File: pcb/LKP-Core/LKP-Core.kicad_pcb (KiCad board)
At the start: 2 copper layers, 41 x 32 mm, 30 parts, among them J1 Intercon L, J2 Intercon R, J3 Power JST PH, J4 IO, J5 SWD, U1 CY8C4246AZI-M445

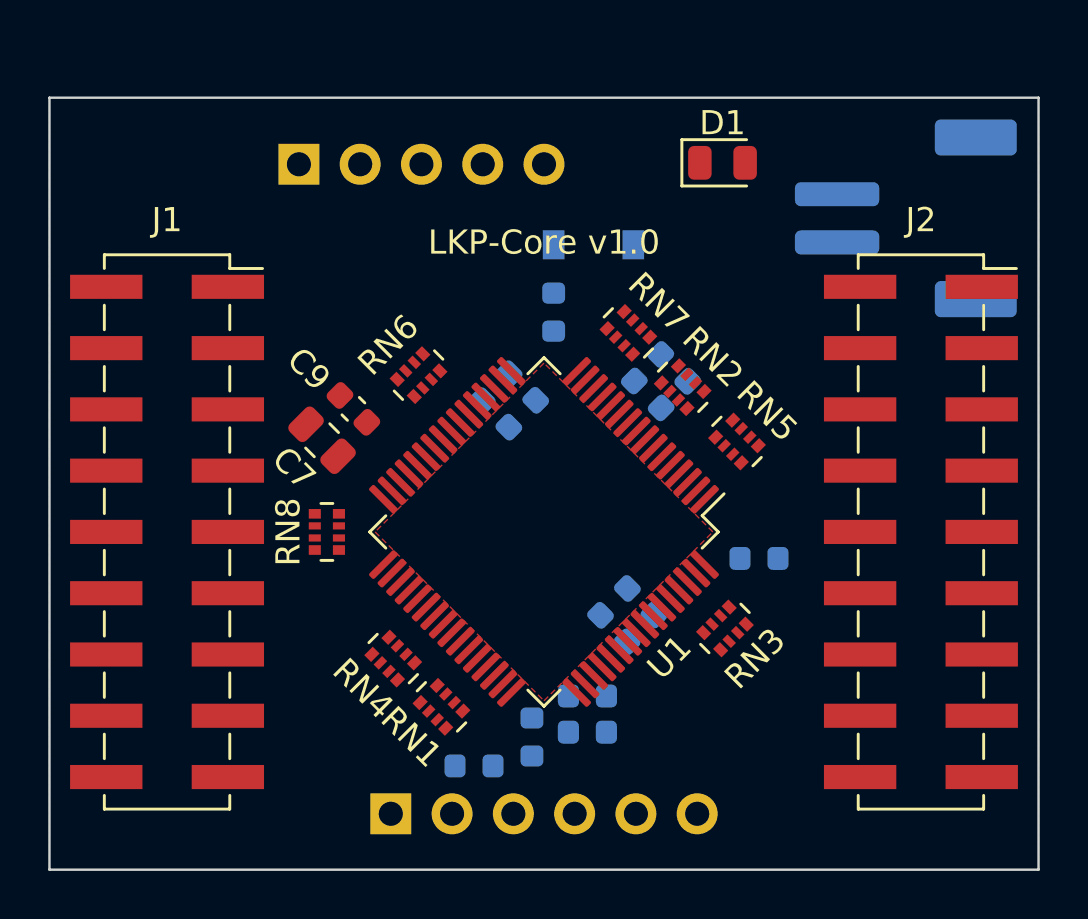
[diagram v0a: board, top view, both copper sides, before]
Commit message: Define net classes
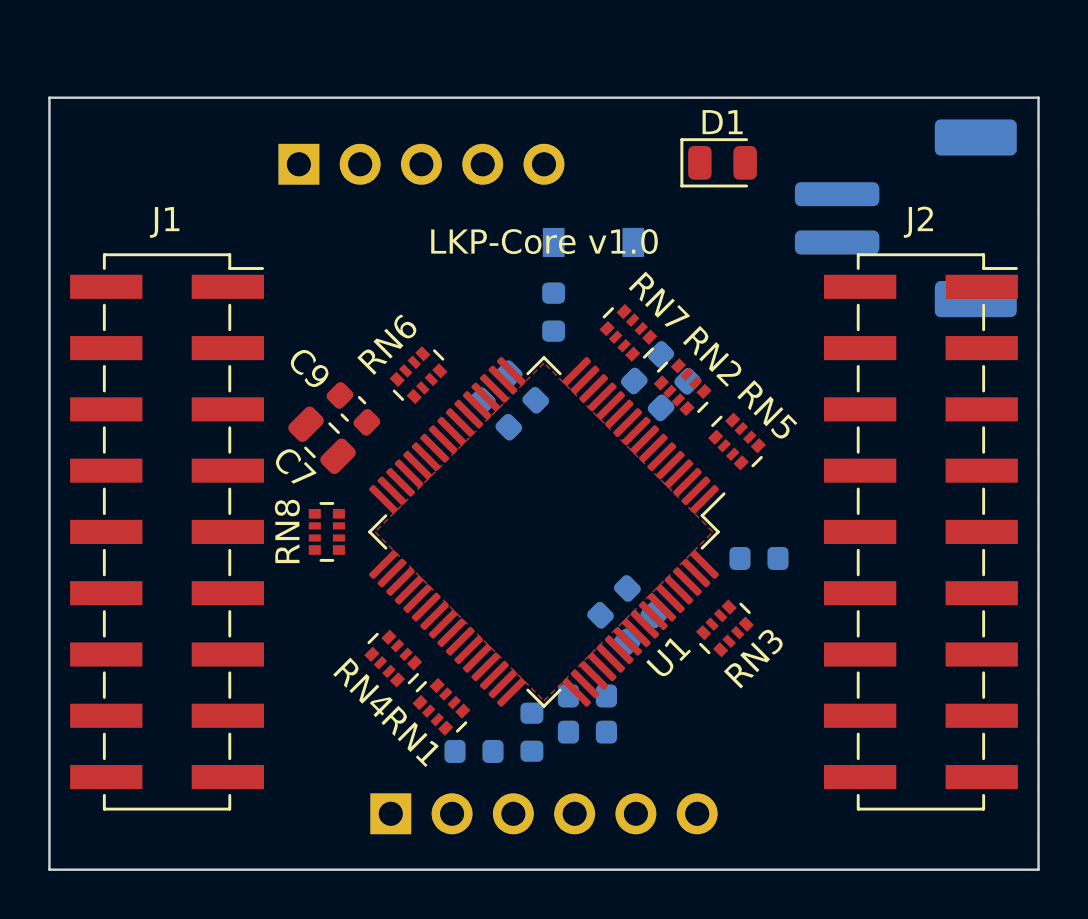
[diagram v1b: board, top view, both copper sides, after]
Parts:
- moved R2 0.60 mm to (144.0, 107.1)
- moved C2 0.20 mm to (146.4, 106.3)
- moved D2 0.10 mm to (148.9, 86.0)
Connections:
- J3 pad 2: Net-(J3-Pad2) -> +5V
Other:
- net class CapSense added: clearance 0.127, trace_width 0.1524, via_dia 0.6, via_drill 0.3
- net class Default: clearance 0.2 -> 0.127; trace_width 0.25 -> 0.2
- net class Power added: clearance 0.127, trace_width 0.5, via_dia 0.8, via_drill 0.4
- rule trace_clearance: 0.2 -> 0.127
- rule trace_min: 0.2 -> 0.127
- rule via_min_size: 0.4 -> 0.6
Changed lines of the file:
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@@
     (zones 0)
     (modules 30)
-    (nets 93)
+    (nets 92)
   )
   (page A4)
@@
   )
   (setup
-    (last_trace_width 0.25)
-    (trace_clearance 0.2)
+    (last_trace_width 0.2)
+    (user_trace_width 0.2)
+    (trace_clearance 0.127)
     (zone_clearance 0.508)
     (zone_45_only no)
-    (trace_min 0.2)
+    (trace_min 0.127)
     (via_size 0.8)
     (via_drill 0.4)
-    (via_min_size 0.4)
+    (via_min_size 0.6)
     (via_min_drill 0.3)
     (uvia_size 0.3)
@@
   (net 90 "Net-(U1-Pad1)")
   (net 91 "Net-(D2-Pad1)")
-  (net 92 "Net-(J3-Pad2)")
   (net_class Default "This is the default net class."
-    (clearance 0.2)
-    (trace_width 0.25)
+    (clearance 0.127)
+    (trace_width 0.2)
     (via_dia 0.8)
     (via_drill 0.4)
     (uvia_dia 0.3)
     (uvia_drill 0.1)
-    (add_net +5V)
     (add_net /CMOD)
     (add_net /CSH)
+    (add_net /I2C_SCL)
+    (add_net /I2C_SDA)
+    (add_net /INT)
+    (add_net /LED)
+    (add_net /LED_STAT)
+    (add_net /RESET)
+    (add_net /S0_SH)
+    (add_net /S1_SH)
+    (add_net /SWCLK)
+    (add_net /SWDIO)
+    (add_net GND)
+    (add_net "Net-(C2-Pad1)")
+    (add_net "Net-(D1-Pad2)")
+    (add_net "Net-(D2-Pad1)")
+    (add_net "Net-(R2-Pad2)")
+    (add_net "Net-(U1-Pad1)")
+    (add_net "Net-(U1-Pad51)")
+    (add_net "Net-(U1-Pad52)")
+    (add_net "Net-(U1-Pad53)")
+    (add_net "Net-(U1-Pad54)")
+    (add_net "Net-(U1-Pad55)")
+    (add_net "Net-(U1-Pad58)")
+    (add_net "Net-(U1-Pad59)")
+    (add_net VDD)
+  )
+  (net_class CapSense ""
+    (clearance 0.127)
+    (trace_width 0.1524)
+    (via_dia 0.6)
+    (via_drill 0.3)
+    (uvia_dia 0.3)
+    (uvia_drill 0.1)
     (add_net /E0_0)
     (add_net /E0_1)
@@
     (add_net /E1_8)
     (add_net /E1_9)
-    (add_net /I2C_SCL)
-    (add_net /I2C_SDA)
-    (add_net /INT)
-    (add_net /LED)
-    (add_net /LED_STAT)
-    (add_net /RESET)
     (add_net /S0_0)
     (add_net /S0_1)
@@
     (add_net /S0_8)
     (add_net /S0_9)
-    (add_net /S0_SH)
     (add_net /S1_0)
     (add_net /S1_1)
@@
     (add_net /S1_8)
     (add_net /S1_9)
-    (add_net /S1_SH)
-    (add_net /SWCLK)
-    (add_net /SWDIO)
-    (add_net GND)
-    (add_net "Net-(C2-Pad1)")
-    (add_net "Net-(D1-Pad2)")
-    (add_net "Net-(D2-Pad1)")
-    (add_net "Net-(J3-Pad2)")
-    (add_net "Net-(R2-Pad2)")
-    (add_net "Net-(U1-Pad1)")
-    (add_net "Net-(U1-Pad51)")
-    (add_net "Net-(U1-Pad52)")
-    (add_net "Net-(U1-Pad53)")
-    (add_net "Net-(U1-Pad54)")
-    (add_net "Net-(U1-Pad55)")
-    (add_net "Net-(U1-Pad58)")
-    (add_net "Net-(U1-Pad59)")
-    (add_net VDD)
+  )
+  (net_class Power ""
+    (clearance 0.127)
+    (trace_width 0.5)
+    (via_dia 0.8)
+    (via_drill 0.4)
+    (uvia_dia 0.3)
+    (uvia_drill 0.1)
+    (add_net +5V)
   )
   (module Connector_PinHeader_2.54mm:PinHeader_1x05_P2.54mm_Vertical (layer B.Cu)
@@
   )
   (module Resistor_SMD:R_0603_1608Metric (layer B.Cu)
-    (at 143.975 107.7)
+    (at 143.975 107.1)
     (descr "Resistor SMD 0603 (1608 Metric), square (rectangular) end terminal, IPC_7351 nominal, (Body size source: http://www.tortai-tech.com/upload/download/2011102023233369053.pdf), generated with kicad-footprint-generator")
     (tags resistor)
@@
     (pad MP smd roundrect (at -3.35 -2.9 270) (size 1.5 3.4) (layers B.Cu B.Paste B.Mask) (roundrect_rratio 0.166667))
     (pad 2 smd roundrect (at 1 2.85 270) (size 1 3.5) (layers B.Cu B.Paste B.Mask) (roundrect_rratio 0.25)
-      (net 92 "Net-(J3-Pad2)"))
+      (net 7 +5V))
     (pad 1 smd roundrect (at -1 2.85 270) (size 1 3.5) (layers B.Cu B.Paste B.Mask) (roundrect_rratio 0.25)
       (net 1 GND))
@@
   )
   (module Diode_SMD:D_SOD-123 (layer B.Cu)
-    (at 148.925 86.1)
+    (at 148.925 86)
     (descr SOD-123)
     (tags SOD-123)
@@
   )
   (module Capacitor_SMD:C_0603_1608Metric (layer B.Cu)
-    (at 146.375 106.5 270)
+    (at 146.375 106.3 270)
     (descr "Capacitor SMD 0603 (1608 Metric), square (rectangular) end terminal, IPC_7351 nominal, (Body size source: http://www.tortai-tech.com/upload/download/2011102023233369053.pdf), generated with kicad-footprint-generator")
     (tags capacitor)

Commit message: Power routing plan
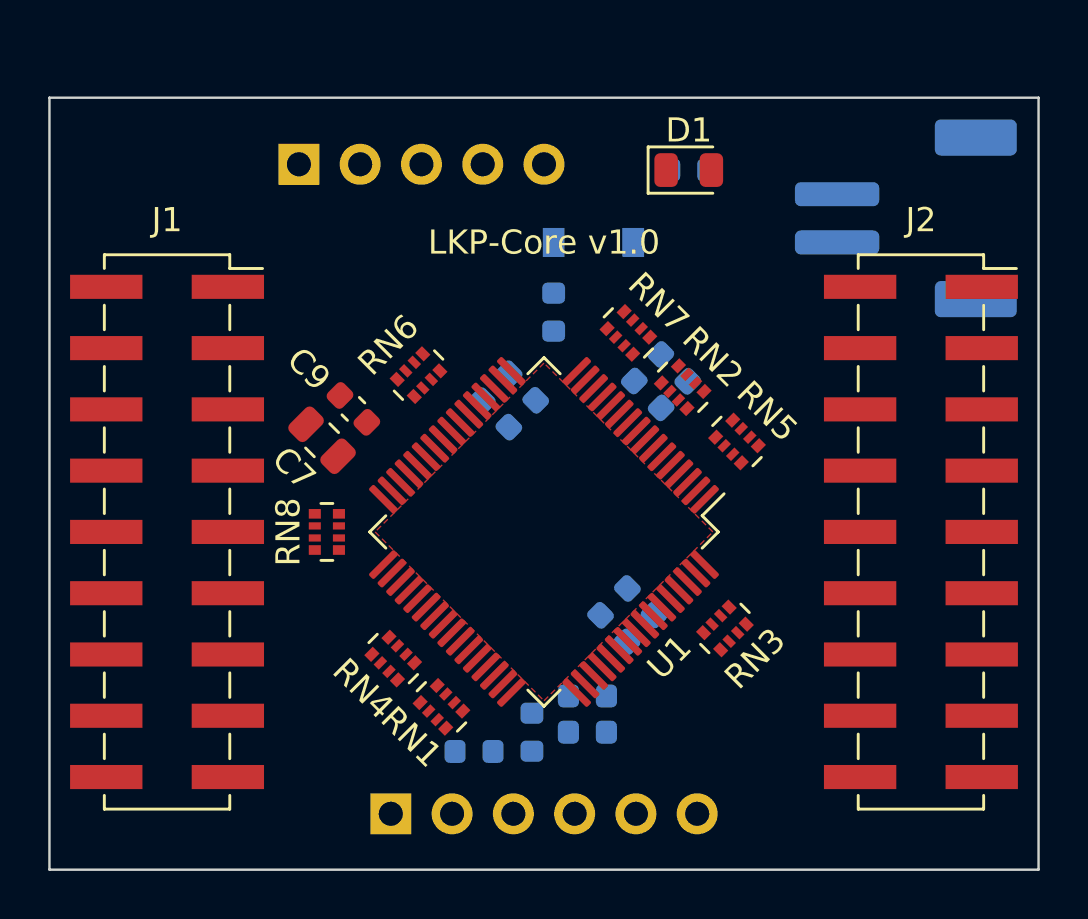
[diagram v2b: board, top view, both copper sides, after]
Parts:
- moved R1 16.4 mm to (152.9, 83.0)
- moved D1 1.43 mm to (152.9, 83.0)
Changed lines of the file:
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@@
   (general
     (thickness 1.6)
-    (drawings 13)
+    (drawings 28)
     (tracks 0)
     (zones 0)
@@
   )
   (module Resistor_SMD:R_0603_1608Metric (layer B.Cu)
-    (at 155.7875 99.1)
+    (at 152.875 83)
     (descr "Resistor SMD 0603 (1608 Metric), square (rectangular) end terminal, IPC_7351 nominal, (Body size source: http://www.tortai-tech.com/upload/download/2011102023233369053.pdf), generated with kicad-footprint-generator")
     (tags resistor)
@@
   )
   (module LED_SMD:LED_0805_2012Metric (layer F.Cu)
-    (at 154.275 82.7)
+    (at 152.875 83)
     (descr "LED SMD 0805 (2012 Metric), square (rectangular) end terminal, IPC_7351 nominal, (Body size source: https://docs.google.com/spreadsheets/d/1BsfQQcO9C6DZCsRaXUlFlo91Tg2WpOkGARC1WS5S8t0/edit?usp=sharing), generated with kicad-footprint-generator")
     (tags diode)
@@
     )
   )
-  (gr_line (start 151.275 103.6) (end 150.175 102.8) (layer Dwgs.User) (width 0.15))
-  (gr_line (start 156.275 97.5) (end 151.275 103.6) (layer Dwgs.User) (width 0.15))
-  (gr_line (start 147.175 85.9) (end 147.275 88.3) (layer Dwgs.User) (width 0.15))
-  (gr_line (start 150.675 86.2) (end 158.975 86.1) (layer Dwgs.User) (width 0.15))
-  (gr_line (start 150.675 80.7) (end 150.675 86.2) (layer Dwgs.User) (width 0.15))
-  (gr_line (start 136.775 80.7) (end 150.675 80.7) (layer Dwgs.User) (width 0.15))
+  (gr_line (start 146.275 105.5) (end 145.575 104.7) (layer Cmts.User) (width 0.15))
+  (gr_line (start 149.475 106.6) (end 149.575 105) (layer Cmts.User) (width 0.15))
+  (gr_line (start 151.275 103.4) (end 149.475 106.6) (layer Cmts.User) (width 0.15))
+  (gr_line (start 151.275 103.4) (end 150.475 102.7) (layer Cmts.User) (width 0.15))
+  (gr_line (start 153.775 101.1) (end 151.275 103.4) (layer Cmts.User) (width 0.15))
+  (gr_line (start 157.275 94.5) (end 153.775 101.1) (layer Cmts.User) (width 0.15))
+  (gr_line (start 152.875 89.8) (end 157.275 94.5) (layer Cmts.User) (width 0.15))
+  (gr_line (start 151.775 90.9) (end 152.875 89.8) (layer Cmts.User) (width 0.15))
+  (gr_line (start 148.475 89.8) (end 151.675 90.8) (layer Cmts.User) (width 0.15))
+  (gr_line (start 147.175 89.7) (end 148.475 89.8) (layer Cmts.User) (width 0.15))
+  (gr_line (start 151.775 90.9) (end 150.575 91.9) (layer Cmts.User) (width 0.15))
+  (gr_line (start 144.175 92.6) (end 145.475 93.7) (layer Cmts.User) (width 0.15))
+  (gr_line (start 143.575 91.9) (end 144.175 92.6) (layer Cmts.User) (width 0.15))
+  (gr_line (start 145.375 90) (end 143.575 91.9) (layer Cmts.User) (width 0.15))
+  (gr_line (start 147.275 89.7) (end 145.375 90) (layer Cmts.User) (width 0.15))
+  (gr_line (start 147.275 86.1) (end 147.275 88.2) (layer Cmts.User) (width 0.15))
+  (gr_line (start 152.775 86) (end 150.475 86) (layer Cmts.User) (width 0.15))
+  (gr_line (start 152.775 86) (end 158.475 85.9) (layer Cmts.User) (width 0.15))
+  (gr_line (start 152.775 80.9) (end 152.775 86) (layer Cmts.User) (width 0.15))
+  (gr_line (start 136.675 80.9) (end 152.775 80.9) (layer Cmts.User) (width 0.15))
+  (gr_line (start 136.675 82.8) (end 136.675 80.9) (layer Cmts.User) (width 0.15))
   (gr_line (start 126.375 112) (end 126.375 80) (layer Edge.Cuts) (width 0.1))
   (gr_line (start 167.375 112) (end 126.375 112) (layer Edge.Cuts) (width 0.1))

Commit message: Power line routing
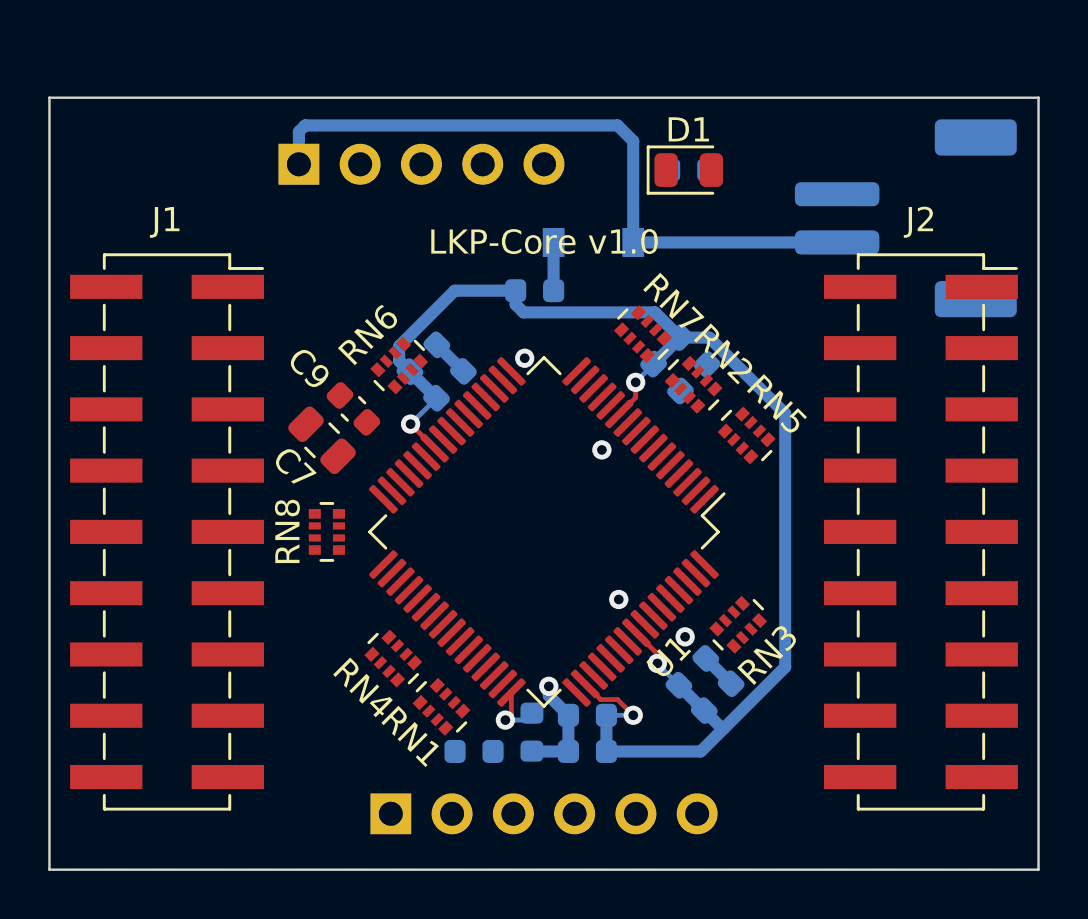
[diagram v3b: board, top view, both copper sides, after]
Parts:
- moved C10 4.70 mm to (141.9, 90.8)
- moved C6 4.36 mm to (153.0, 103.8)
- moved C8 4.29 mm to (154.1, 104.8)
- moved C11 1.90 mm to (143.0, 91.9)
- moved FB1 1.19 mm to (146.5, 88.0), turned to 0 degrees
- moved C4 1.06 mm to (152.0, 91.6)
- moved C5 1.06 mm to (153.1, 90.5)
- moved RN6 0.89 mm to (140.9, 91.1)
- moved C1 0.80 mm to (148.7, 105.6)
- moved C3 0.80 mm to (148.7, 107.1)
- moved RN7 0.60 mm to (151.0, 89.8)
- moved RN3 0.57 mm to (154.9, 101.8)
- moved RN5 0.47 mm to (155.3, 94.0)
- moved RN2 0.46 mm to (153.1, 91.9)
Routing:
- net VDD: track 0.00 -> 59.4 mm, vias 0 -> 4
- net +5V: track 0.00 -> 28.2 mm
- net GND: track 0.00 -> 7.59 mm, vias 0 -> 5
- net Net-(C2-Pad1): track 0.00 -> 2.47 mm, vias 0 -> 1
- net Net-(D2-Pad1): track 0.00 -> 2.00 mm

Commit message: Sensor routing
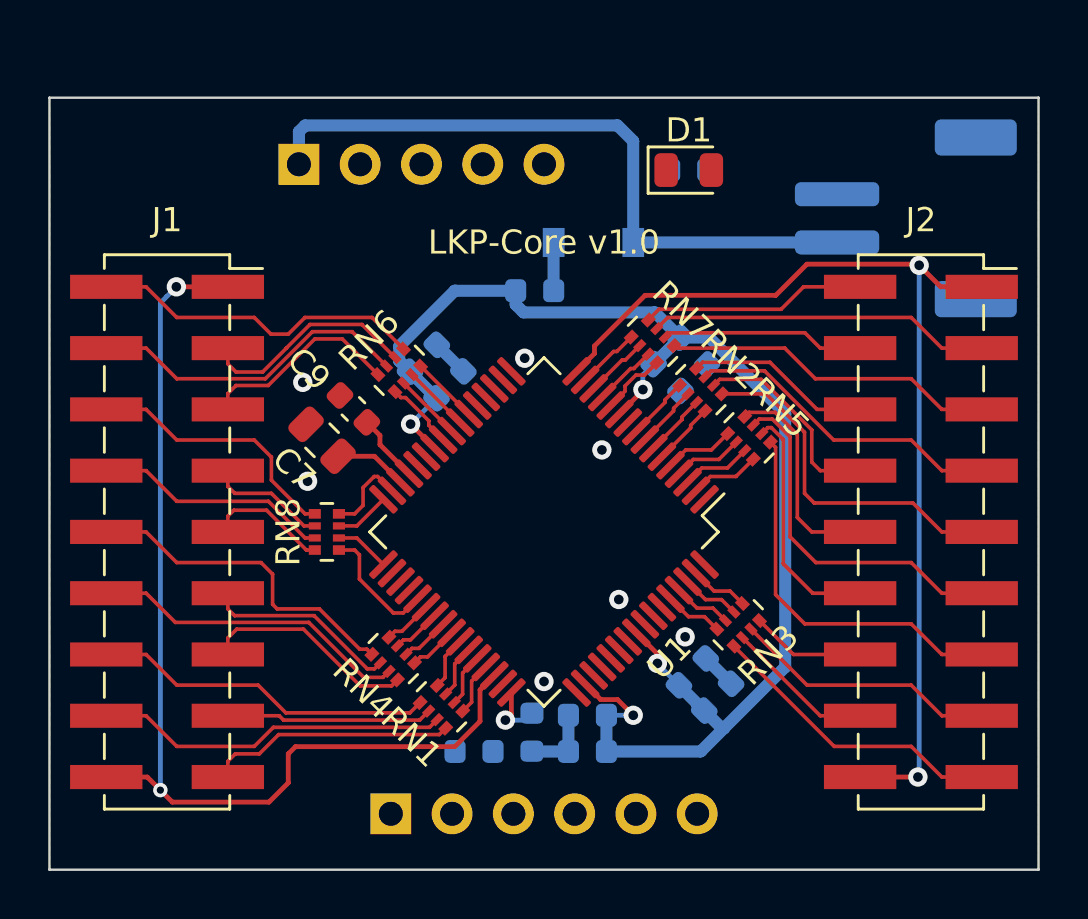
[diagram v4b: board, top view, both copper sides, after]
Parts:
- moved RN7 0.50 mm to (151.4, 90.1)
- moved RN2 0.36 mm to (153.4, 92.1)
- moved RN6 0.20 mm to (140.9, 91.3)
- moved RN5 0.14 mm to (155.4, 94.1)
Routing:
- net /S0_SH: track 0.00 -> 43.4 mm, vias 0 -> 2
- net /S1_SH: track 0.00 -> 42.8 mm, vias 0 -> 2
- net /E1_4: track 0.00 -> 16.0 mm
- net /E1_6: track 0.00 -> 15.0 mm
- net /E0_14: track 0.00 -> 14.7 mm
- net /E1_8: track 0.00 -> 14.6 mm
- net /E0_12: track 0.00 -> 14.2 mm
- net /E1_14: track 0.00 -> 14.2 mm
- net /E0_0: track 0.00 -> 14.0 mm
- net /E1_12: track 0.00 -> 13.9 mm
- net /E0_8: track 0.00 -> 13.8 mm
- net /E0_2: track 0.00 -> 13.5 mm
- net /E1_10: track 0.00 -> 13.3 mm
- net /E0_10: track 0.00 -> 13.3 mm
- net /E1_0: track 0.00 -> 12.5 mm
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
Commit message: Finishing up
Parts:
- removed the D1 at (152.9, 83.0)
- removed R1: 1k, Resistor_SMD:R_0603_1608Metric
- moved R2 1.70 mm to (142.3, 107.1), turned to 180 degrees
- moved C7 0.60 mm to (138.3, 94.2)
- moved C9 0.50 mm to (139.5, 92.9)
- moved RN2 0.10 mm to (153.4, 92.2)
- moved RN5 0.10 mm to (155.4, 94.2)
- moved RN7 0.10 mm to (151.3, 90.1)
- renumbered D2 to D1
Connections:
- U1 pad 64: /LED_STAT -> Net-(U1-Pad64)
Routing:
- net /RESET: track 0.00 -> 40.3 mm, vias 0 -> 2
- net /INT: track 0.00 -> 27.1 mm, vias 0 -> 1
- net /I2C_SDA: track 0.00 -> 26.0 mm, vias 0 -> 1
- net /I2C_SCL: track 0.00 -> 25.6 mm, vias 0 -> 1
- net Net-(R2-Pad2): track 0.00 -> 19.8 mm, vias 0 -> 1
- net /SWDIO: track 0.00 -> 16.8 mm, vias 0 -> 1
- net /SWCLK: track 0.00 -> 15.7 mm, vias 0 -> 1
- net /LED: track 0.00 -> 2.58 mm
- net /E1_12: track 13.9 -> 14.5 mm
- net /CSH: track 3.03 -> 2.43 mm
- net GND: vias 7 -> 63

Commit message: Apply changes
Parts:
- added J6: WS281x, Connector_PinHeader_2.54mm:PinHeader_1x02_P2.54mm_Vertical, F.Cu at (129.3, 80.5)
- J4: footprint Connector_PinHeader_2.54mm:PinHeader_1x06_P2.54mm_Vertical -> Connector_PinHeader_2.54mm:PinHeader_1x04_P2.54mm_Vertical; moved to F.Cu
- R2: moved to F.Cu
- moved R2 25.8 mm to (132.9, 83.0), turned to 0 degrees
- moved J4 2.55 mm to (143.1, 109.4), turned to 90 degrees
- moved RN3 0.29 mm to (155.1, 101.6)
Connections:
- J4 pad 2: /LED -> /INT
- J4 pad 3: GND -> /I2C_SCL
- J4 pad 4: /INT -> /I2C_SDA
- U1 pad 18: /INT -> Net-(U1-Pad18)
- U1 pad 27: /I2C_SCL -> Net-(U1-Pad27)
- U1 pad 28: /I2C_SDA -> Net-(U1-Pad28)
- U1 pad 52: Net-(U1-Pad52) -> /INT
- U1 pad 58: Net-(U1-Pad58) -> /I2C_SCL
- U1 pad 59: Net-(U1-Pad59) -> /I2C_SDA
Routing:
- net /INT: track 27.1 -> 11.5 mm, vias 1 -> 0
- net /I2C_SDA: track 26.0 -> 11.3 mm, vias 1 -> 0
- net /I2C_SCL: track 25.6 -> 13.3 mm, vias 1 -> 0
- net Net-(R2-Pad2): track 19.8 -> 14.9 mm, vias 1 -> 0
- net GND: vias 63 -> 51
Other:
- board size 41 x 32 mm -> 41 x 34 mm
